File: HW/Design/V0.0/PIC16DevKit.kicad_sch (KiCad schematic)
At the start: 0 parts

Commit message: PIC16-DevKit-PCB-877 PCB V0.0
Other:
- company: (none) -> SAMPI DEVELOPMENT KITS
- title: (none) -> PIC16F877A DEV KIT

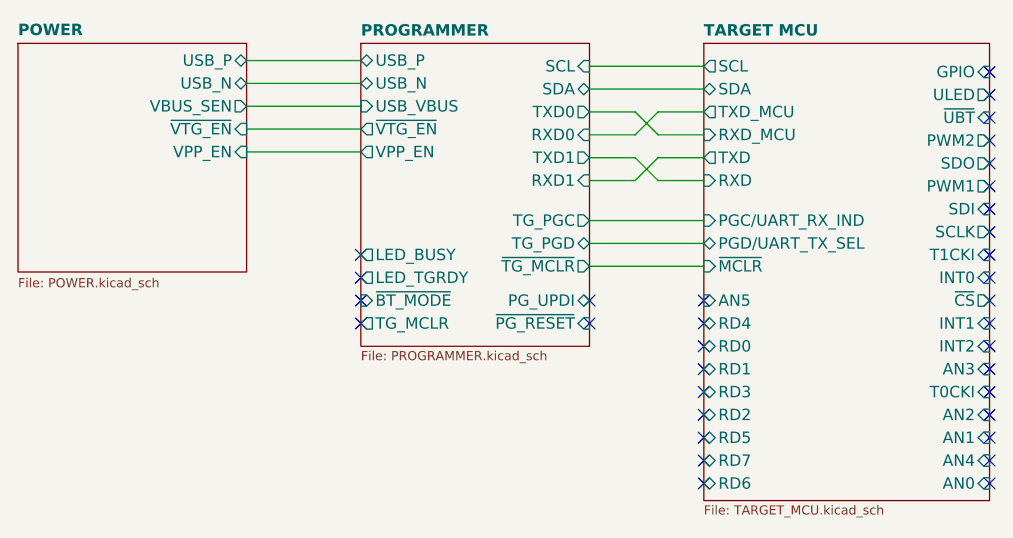
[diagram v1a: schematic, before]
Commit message: PIC16-DevKit-PCB-877 V0.1 - QWIIC ESD protection, disable VPP, detect VBUS, measure VPP, VDDTG
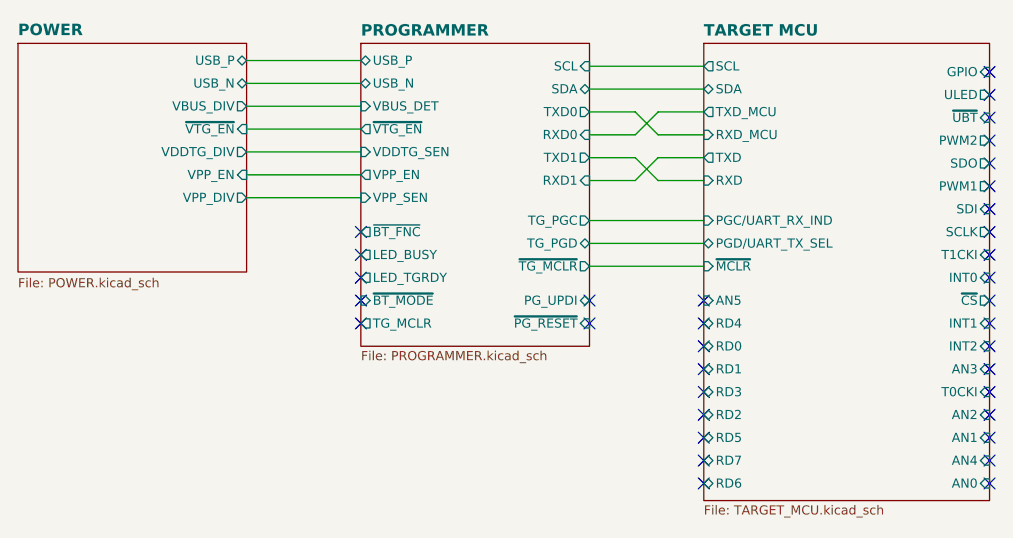
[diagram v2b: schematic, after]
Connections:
- no-connect marks 34 -> 35
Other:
- sheet POWER ports: added VBUS_DIV, VDDTG_DIV, VPP_DIV; removed VBUS_SEN
- sheet PROGRAMMER ports: added VBUS_DET, VDDTG_SEN, VPP_SEN, ~{BT_FNC}; removed USB_VBUS
